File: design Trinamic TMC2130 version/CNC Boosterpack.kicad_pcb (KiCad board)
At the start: 4 copper layers, 58.4 x 62.5 mm, 73 parts, among them J1 SBW, J10 EEPROMaddr, J11 UART/GPIO, J4 I2CDrv, J5 I2C, J6 RESET, J7 VDrvGND, J8 VDrvSel, J9 Spindle/Coolant, P1 CONN_02x10, P10 XC, P12 YA, P13 YB, P14 ZA, P15 ZB, P17 VMOT, P2 GPIO, P3 Control, P4 ZC, P5 YC, P6 XB, P7 CONN_02x10, P8 Limits, P9 XA, Q1 2N7002, Q2 2N7002, Q3 2N7002, Q4 2N7002, U1 TLP290-4, U2 TLP290-4, U3 TLP290-4, U4 24LC16, U5 TCA9406, U6 MSP430G2553-20

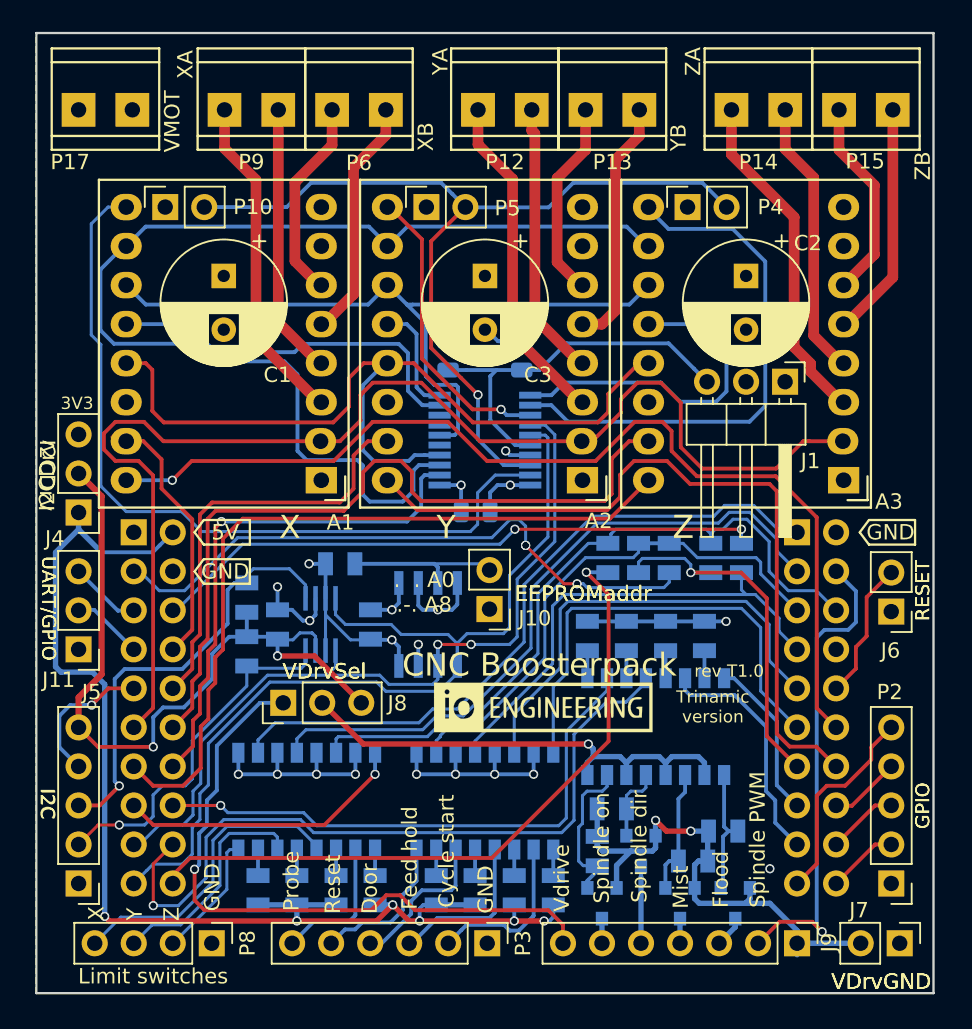
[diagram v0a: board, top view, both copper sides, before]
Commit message: Updated to latest revision
A small batch of the Trinamic-version PCB has been made, driver
development in good progress. Marlin-style M-commands will be supported
including status reports. Grbl protocol extensions allows real-trime
plotting of data (stallguard value) for simpler tuning.
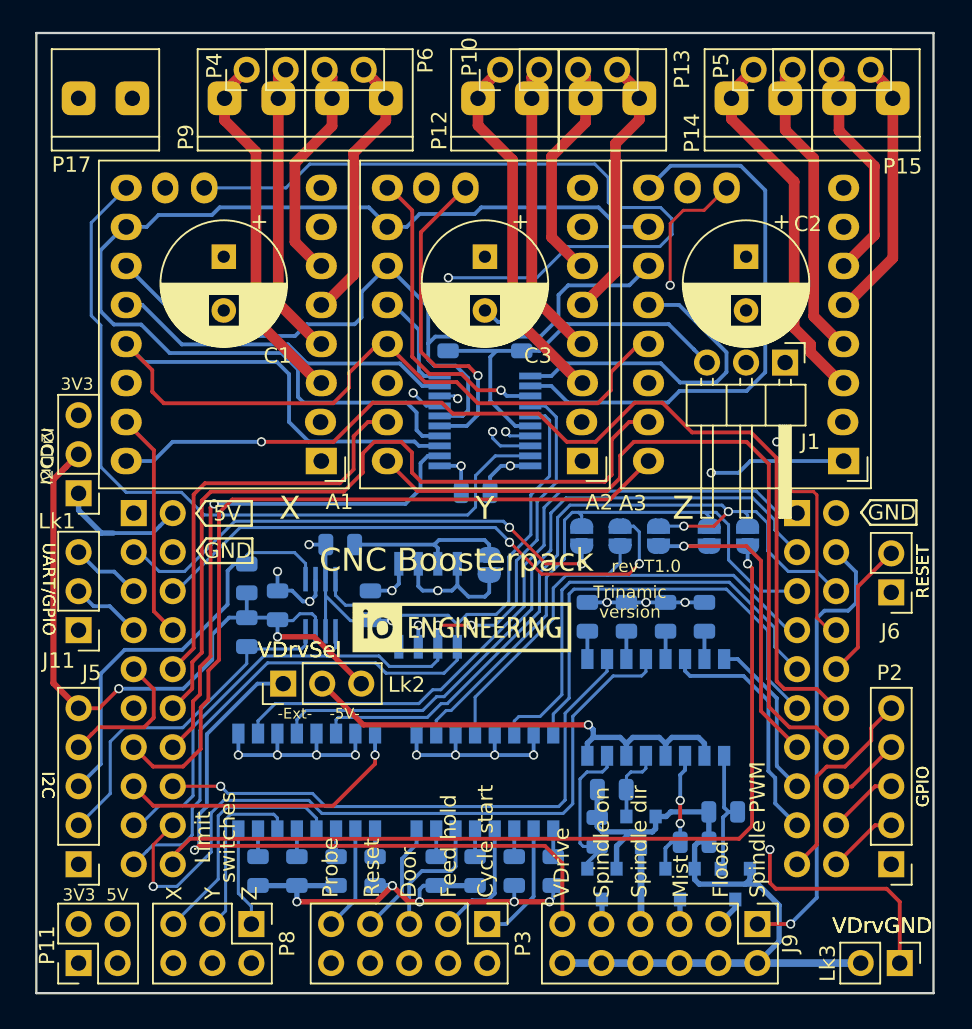
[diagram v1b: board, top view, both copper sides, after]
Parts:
- removed J10: EEPROMaddr, Connector_PinHeader_2.54mm:PinHeader_1x02_P2.54mm_Vertical
- removed R10, R11, R12, R13, R14: 0R, Resistor_SMD:R_0805_2012Metric
- added J12: Lk, Jumper:SolderJumper-2_P1.3mm_Open_RoundedPad1.0x1.5mm, B.Cu at (40.5, -29.8)
- added J13: Lk, Jumper:SolderJumper-2_P1.3mm_Open_RoundedPad1.0x1.5mm, B.Cu at (46.3, -29.8)
- added J14: Lk, Jumper:SolderJumper-2_P1.3mm_Open_RoundedPad1.0x1.5mm, B.Cu at (43.8, -29.8)
- added J2: Lk, Jumper:SolderJumper-2_P1.3mm_Open_RoundedPad1.0x1.5mm, B.Cu at (35.5, -29.8)
- added J3: Lk, Jumper:SolderJumper-2_P1.3mm_Open_RoundedPad1.0x1.5mm, B.Cu at (38.0, -29.8)
- added Lk4: EEPROMaddr, Jumper:SolderJumper-2_P1.3mm_Open_RoundedPad1.0x1.5mm, B.Cu at (29.5, -27.9)
- added P11: Power, Connector_PinHeader_2.54mm:PinHeader_2x02_P2.54mm_Vertical, F.Cu at (2.75, -1.96)
- A1, A2, A3: value Pololu_Breakout_DRV8825 -> SilentStepStick_Breakout_TMC2130; footprint IoEngineering:Polulu_A4988 -> IoEngineering:SilentStepStick_TMC2130
- J9: footprint Connector_PinHeader_2.54mm:PinHeader_1x07_P2.54mm_Vertical -> Connector_PinHeader_2.54mm:PinHeader_2x06_P2.54mm_Vertical
- P1: value CONN_02x10 -> BP A-B
- P10: value XC -> YMotor; footprint Connector_PinSocket_2.54mm:PinSocket_1x02_P2.54mm_Vertical -> IoEngineering:PinHeader_1x04_P2.54mm_Vertical_Motor
- P12, P13, P14, P15, P17, P6, P9: footprint IoEngineering:CONN_PWR_2P_3.5MM -> IoEngineering:CONN_PWR_2P_3.5MM_CAMBLOCK
- P3: footprint Connector_PinHeader_2.54mm:PinHeader_1x06_P2.54mm_Vertical -> Connector_PinHeader_2.54mm:PinHeader_2x05_P2.54mm_Vertical
- P4: value ZC -> XMotor; footprint Connector_PinSocket_2.54mm:PinSocket_1x02_P2.54mm_Vertical -> IoEngineering:PinHeader_1x04_P2.54mm_Vertical_Motor
- P5: value YC -> ZMotor; footprint Connector_PinSocket_2.54mm:PinSocket_1x02_P2.54mm_Vertical -> IoEngineering:PinHeader_1x04_P2.54mm_Vertical_Motor
- P7: value CONN_02x10 -> BP C-D
- P8: footprint Connector_PinHeader_2.54mm:PinHeader_1x04_P2.54mm_Vertical -> Connector_PinHeader_2.54mm:PinHeader_2x03_P2.54mm_Vertical
- moved P4 30.1 mm to (13.7, -60.1)
- moved P10 23.6 mm to (30.2, -60.1)
- moved P5 23.1 mm to (46.7, -60.1)
- moved G*** 7.43 mm to (27.7, -23.8)
- moved J9 2.87 mm to (46.9, -4.50)
- moved P8 2.87 mm to (14.0, -4.50)
- moved REF** 1.36 mm to (12.5, -28.8)
- moved REF** 1.29 mm to (55.7, -31.3)
- moved Lk3 1.29 mm to (56.2, -1.96)
- moved J5 1.25 mm to (2.75, -8.39)
- moved P2 1.25 mm to (55.6, -8.39)
- moved A1 1.25 mm to (18.6, -34.6)
- moved A2 1.25 mm to (35.5, -34.6)
- moved A3 1.25 mm to (52.5, -34.6)
- moved C1 1.25 mm to (12.2, -47.9)
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- renumbered J4 to Lk1, J8 to Lk2, J7 to Lk3
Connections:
- net /VBUS renamed VBUS
- net /VCCB renamed VCCQ
- net /VMOT renamed VDDF
- A1 pad 10: /SDI -> Net-(A1-Pad10)
- A1 pad 11: /SCK -> /ENX
- A1 pad 12: /~CSX -> /SDI
- A1 pad 13: /SDO -> /SCK
- A1 pad 14: /3V3 -> /~CSX
- A1 pad 15: /PD1 -> /SDO
- A1 pad 16: /PB7 -> Net-(A1-Pad16)
- A1 pad 2: /PE5 -> +3V3
- A1 pad 9: /ENX -> /DIAGX
- A2 pad 10: /SDI -> Net-(A2-Pad10)
- A2 pad 11: /SCK -> /ENY
- A2 pad 12: /~CSY -> /SDI
- A2 pad 13: /SDO -> /SCK
- A2 pad 14: /3V3 -> /~CSY
- A2 pad 15: /PD2 -> /SDO
- A2 pad 16: /PB6 -> Net-(A2-Pad16)
- A2 pad 2: /PE5 -> +3V3
- A2 pad 9: /ENY -> /DIAGY
- A3 pad 10: /SDI -> Net-(A3-Pad10)
- A3 pad 11: /SCK -> /ENZ
- A3 pad 12: /~CSZ -> /SDI
- A3 pad 13: /SDO -> /SCK
- A3 pad 14: /3V3 -> /~CSZ
- A3 pad 15: /PD3 -> /SDO
- A3 pad 16: /PB4 -> Net-(A3-Pad16)
- A3 pad 2: /PE5 -> +3V3
- A3 pad 9: /ENZ -> /DIAGZ
- C4 pad 1: /3V3 -> +3V3
- C7 pad 1: /3V3 -> +3V3
- J9 pad 1: Net-(J7-Pad2) -> /PB2
- J9 pad 2: /PB2 -> Net-(J9-Pad10)
- J9 pad 4: Net-(J9-Pad4) -> Net-(J9-Pad10)
- J9 pad 6: Net-(J9-Pad6) -> Net-(J9-Pad10)
- J9 pad 7: Net-(J8-Pad1) -> Net-(J9-Pad7)
- Lk1 pad 3: /3V3 -> +3V3
- Lk2 pad 1: Net-(J8-Pad1) -> Net-(J9-Pad11)
- Lk3 pad 2: Net-(J7-Pad2) -> Net-(J9-Pad10)
- P1 pad 1: /3V3 -> +3V3
- P10 pad 1: Net-(P10-Pad1) -> Net-(A2-Pad3)
- P10 pad 2: /DIAG -> Net-(A2-Pad4)
- P3 pad 1: GND -> /CS
- P3 pad 2: /CS -> GND
- P3 pad 4: /SD -> GND
- P3 pad 5: /Reset -> /SD
- P3 pad 6: /Probe -> GND
- P4 pad 1: Net-(P4-Pad1) -> Net-(A1-Pad3)
- P4 pad 2: /DIAG -> Net-(A1-Pad4)
- P5 pad 1: Net-(P5-Pad1) -> Net-(A3-Pad3)
- P5 pad 2: /DIAG -> Net-(A3-Pad4)
- P8 pad 1: GND -> /LimZ
- P8 pad 2: /LimZ -> GND
- P8 pad 4: /LimX -> GND
- Q1 pad 2: Net-(J7-Pad2) -> Net-(J9-Pad10)
- Q1 pad 3: Net-(J9-Pad6) -> Net-(J9-Pad9)
- Q2 pad 2: Net-(J7-Pad2) -> Net-(J9-Pad10)
- Q3 pad 2: Net-(J7-Pad2) -> Net-(J9-Pad10)
- Q3 pad 3: Net-(J9-Pad4) -> Net-(J9-Pad5)
- Q4 pad 2: Net-(J7-Pad2) -> Net-(J9-Pad10)
- Q4 pad 3: Net-(J9-Pad5) -> Net-(J9-Pad7)
- R1 pad 1: /3V3 -> +3V3
- R15 pad 1: /3V3 -> +3V3
- R16 pad 1: /3V3 -> +3V3
- R17 pad 1: /3V3 -> +3V3
- R18 pad 2: Net-(J7-Pad2) -> Net-(J9-Pad10)
- R19 pad 2: Net-(J7-Pad2) -> Net-(J9-Pad10)
- R20 pad 2: Net-(J7-Pad2) -> Net-(J9-Pad10)
- R21 pad 2: Net-(J7-Pad2) -> Net-(J9-Pad10)
- R24 pad 1: /3V3 -> +3V3
- R25 pad 1: /3V3 -> +3V3
- U4 pad 8: /3V3 -> +3V3
- U5 pad 3: /3V3 -> +3V3
- U5 pad 6: /3V3 -> +3V3
- U6 pad 1: /3V3 -> +3V3
- U6 pad 18: /DIAG -> /DIAGZ
- U6 pad 3: /SDI -> /SDO
- U6 pad 4: /SDO -> /SDI
- U6 pad 5: Net-(U6-Pad5) -> /DIAGY
- U6 pad 7: Net-(U6-Pad7) -> /DIAGX
- U6 pad 8: Net-(U6-Pad8) -> /PF0
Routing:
- net /PE5: track 81.8 -> 0.00 mm
- net /DIAGX: track 0.00 -> 61.7 mm, vias 0 -> 2
- net /DIAG: track 58.0 -> 0.00 mm, vias 1 -> 0
- net Net-(J9-Pad10): track 0.00 -> 49.8 mm
- net /PF0: track 0.00 -> 44.8 mm, vias 0 -> 2
- net Net-(J8-Pad1): track 42.8 -> 0.00 mm, vias 1 -> 0
- net Net-(J9-Pad11): track 0.00 -> 42.7 mm, vias 0 -> 1
- net VDDF: track 0.00 -> 35.1 mm
- net Net-(J7-Pad2): track 34.6 -> 0.00 mm, vias 2 -> 0
- net /DIAGZ: track 0.00 -> 30.0 mm, vias 0 -> 2
- net /3V3: track 27.5 -> 0.00 mm, vias 5 -> 0
- net GND: track 49.7 -> 77.0 mm, vias 15 -> 16
- net +3V3: track 0.00 -> 25.3 mm, vias 0 -> 7
- net /DIAGY: track 0.00 -> 21.6 mm, vias 0 -> 1
- net /SDO: track 55.3 -> 67.3 mm
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- added copper zone on In2.Cu, net +3V3
- removed copper zone on In2.Cu, net /3V3
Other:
- board text added: "-5V-"
- board text added: "-Ext-"
- board text added: "5V"
- board text added: "MSP432 - Tiva -"
- board text added: "VDrive"
- board text removed: "MSP432 Tiva"
- board text removed: "Vdrive"
